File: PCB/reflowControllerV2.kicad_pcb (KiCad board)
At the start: 4 copper layers, 43 x 89 mm, 97 parts, among them J1 CN4, J10 NEXTION_OB, J11 PWR, J12 A-1JB, J2 SSR2, J3 SSR1, J4 FAN1, J5 FAN2, J6 T1, J7 T2, J8 SWD, J9 NEXTION_FRONT, Q1 BSS316NH6327, Q2 BSS316NH6327, Q3 BSS316NH6327, Q4 BSS316NH6327, Q5 BSS316NH6327, SW1 B3F-4055, U1 918-468K2029E50001, U10 ZD24C128A, U2 918-468K2029E50001, U3 AMS1117-3.3, U4 STM32WBxx_QFN48, U5 USBLC6-2SC6, U6 USBLC6-2SC6, U7 CH340G, U8 MAX31855KASA, U9 MAX31855KASA, Y1 NX2016_32MHz, Y2 NX2012_32K768Hz, Y3 12M

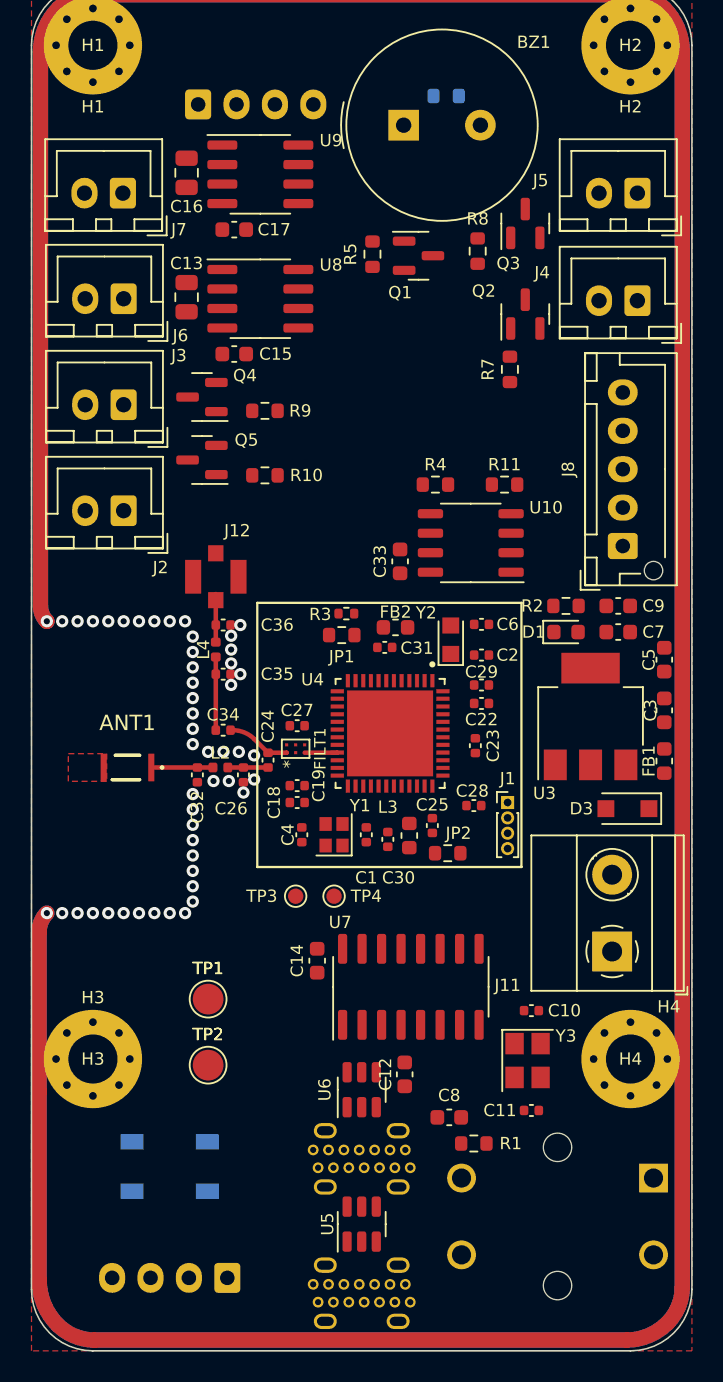
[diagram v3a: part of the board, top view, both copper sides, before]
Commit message: Started layout, critical sections first
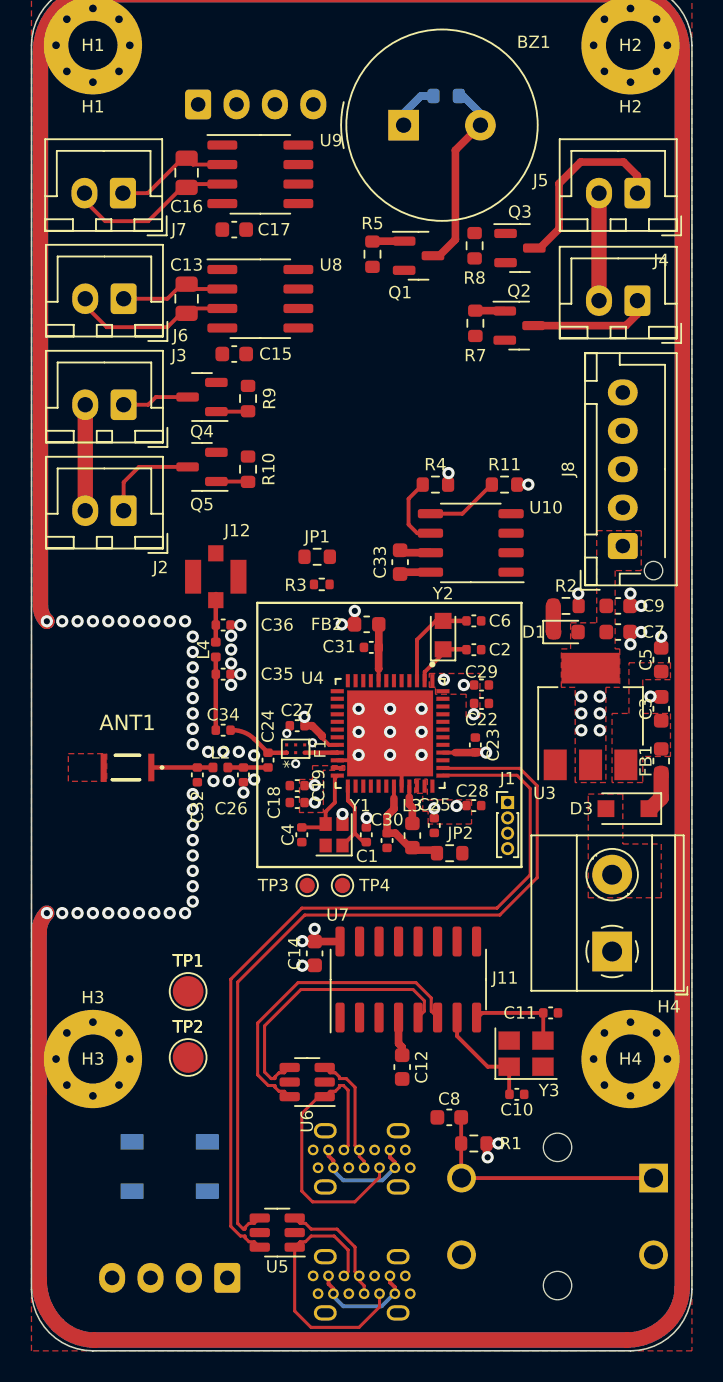
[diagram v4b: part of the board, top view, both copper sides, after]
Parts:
- moved C11 6.47 mm to (33.8, 67.0), turned to 0 degrees
- moved C10 5.53 mm to (31.6, 72.3)
- moved U5 5.53 mm to (16.0, 81.3), turned to 180 degrees
- moved JP1 5.35 mm to (18.6, 37.3)
- moved R7 3.75 mm to (28.9, 22.1)
- moved U6 3.59 mm to (17.9, 71.5), turned to 180 degrees
- moved R3 2.48 mm to (18.9, 39.1)
- moved FB2 1.89 mm to (21.8, 41.7), turned to 0 degrees
- moved Q3 1.64 mm to (31.8, 17.2), turned to 0 degrees
- moved TP1 1.39 mm to (10.2, 65.6)
- moved TP2 1.39 mm to (10.2, 69.9)
- moved R9 1.36 mm to (14.1, 27.0), turned to -90 degrees
- moved R10 1.17 mm to (14.1, 31.6), turned to -90 degrees
- moved TP3 1.03 mm to (17.9, 58.7)
- moved TP4 0.89 mm to (20.2, 58.7)
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- renumbered FILT1 to F1
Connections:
- net Net-(C3-Pad2) renamed /5V_IN
- net Net-(D3-Pad2) renamed /VIN
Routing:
- net /ST_USB_D+: track 0.00 -> 52.6 mm
- net /ST_USB_D-: track 0.00 -> 52.6 mm
- net +3V3: track 0.00 -> 22.0 mm, vias 0 -> 23
- net /UART_USB_D-: track 0.00 -> 20.4 mm
- net /USB2_D-: track 0.00 -> 19.6 mm
- net /UART_USB_D+: track 0.00 -> 18.1 mm
- net /USB1_D-: track 0.00 -> 17.5 mm
- net +5V: track 0.00 -> 16.6 mm
- net /NRST: track 0.00 -> 16.5 mm
- net Net-(BZ1-Pad2): track 0.00 -> 12.7 mm
- net /FAN2: track 0.00 -> 12.3 mm
- net /T2+: track 0.00 -> 11.0 mm
- net /T1+: track 0.00 -> 10.5 mm
- net /USB2_D+: track 0.00 -> 8.06 mm
- net /USB1_D+: track 0.00 -> 7.99 mm
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- added copper zone on F.Cu, net +3V3
- added copper zone on In2.Cu, net +3V3
- added copper zone on F.Cu, net /5V_IN
- added copper zone on F.Cu, net /VIN
- removed copper zone on In2.Cu, net GND

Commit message: Layout done, improovements needed
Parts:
- removed J1: CN4, Connector_PinHeader_1.00mm:PinHeader_1x04_P1.00mm_Vertical
- J10: footprint Connector_JST:JST_XH_S4B-XH-A-1_1x04_P2.50mm_Horizontal -> footprints:JST_254_4P_H
- J2, J3, J4, J5, J6, J7: footprint Connector_JST:JST_XH_B2B-XH-A_1x02_P2.50mm_Vertical -> footprints:JST_254_2P_V
- J8: footprint Connector_JST:JST_XH_B5B-XH-AM_1x05_P2.50mm_Vertical -> footprints:JST_254_5P_V
- J9: footprint Connector_JST:JST_XH_B4B-XH-A_1x04_P2.50mm_Vertical -> footprints:JST_254_4P_V
- moved J12 9.00 mm to (3.00, 38.4), turned to 0 degrees
- moved TP1 7.62 mm to (3.00, 63.1), turned to 90 degrees
- moved TP2 7.39 mm to (7.30, 63.1), turned to 90 degrees
- moved C36 6.93 mm to (6.20, 38.8), turned to 90 degrees
- moved TP4 6.91 mm to (13.5, 57.2)
- moved C35 6.85 mm to (9.40, 38.8), turned to 90 degrees
- moved L4 6.52 mm to (7.80, 38.4), turned to 180 degrees
- moved TP3 5.85 mm to (13.5, 54.9)
- moved Q2 5.06 mm to (32.0, 17.2)
- moved R7 5.06 mm to (29.2, 17.1)
- moved Q3 4.51 mm to (32.0, 21.7)
- moved R8 4.51 mm to (29.1, 21.6)
- moved J2 3.77 mm to (3.25, 31.7), turned to 0 degrees
- moved J3 3.67 mm to (3.25, 25.0), turned to 0 degrees
- moved J6 3.57 mm to (3.25, 18.2), turned to 0 degrees
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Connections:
- J4 pad 1: /FAN1 -> /FAN2
- J5 pad 1: /FAN2 -> /FAN1
- J8 pad 2: /NRST -> /SWDIO
- J8 pad 4: /SWDIO -> /NRST
- U4 pad 26: Net-(J1-Pad1) -> unconnected-(U4-Pad26)
- U4 pad 27: Net-(J1-Pad2) -> unconnected-(U4-Pad27)
- U4 pad 29: /FAN2_IO -> /WS_DATA
- U4 pad 6: /WS_DATA -> /FAN2_IO
- U8 pad 7: /SPI_SO -> /SPI1_MISO
- U9 pad 7: /SPI_SO -> /SPI1_MISO
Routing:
- net +5V: track 16.6 -> 157.5 mm, vias 0 -> 1
- net /USART1_RX: track 0.00 -> 106.5 mm, vias 0 -> 1
- net /USART1_TX: track 0.00 -> 105.4 mm, vias 0 -> 2
- net /NRST: track 16.5 -> 77.3 mm, vias 0 -> 3
- net /SPI1_MISO: track 0.00 -> 42.4 mm
- net /FAN1_IO: track 0.00 -> 41.4 mm, vias 0 -> 2
- net /T2_CS: track 0.00 -> 37.2 mm, vias 0 -> 2
- net /SPI1_SCK: track 0.00 -> 35.1 mm
- net /WS_DATA: track 0.00 -> 33.2 mm, vias 0 -> 1
- net /LPUART1_TX: track 0.00 -> 28.1 mm, vias 0 -> 2
- net /T1_CS: track 0.00 -> 27.9 mm
- net /BUZ: track 0.00 -> 27.1 mm, vias 0 -> 2
- net /LPUART1_RX: track 0.00 -> 26.9 mm, vias 0 -> 2
- net /FAN2_IO: track 0.00 -> 26.3 mm
- net /SWCLK: track 0.00 -> 25.6 mm
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- added copper zone on B.Cu, net GND

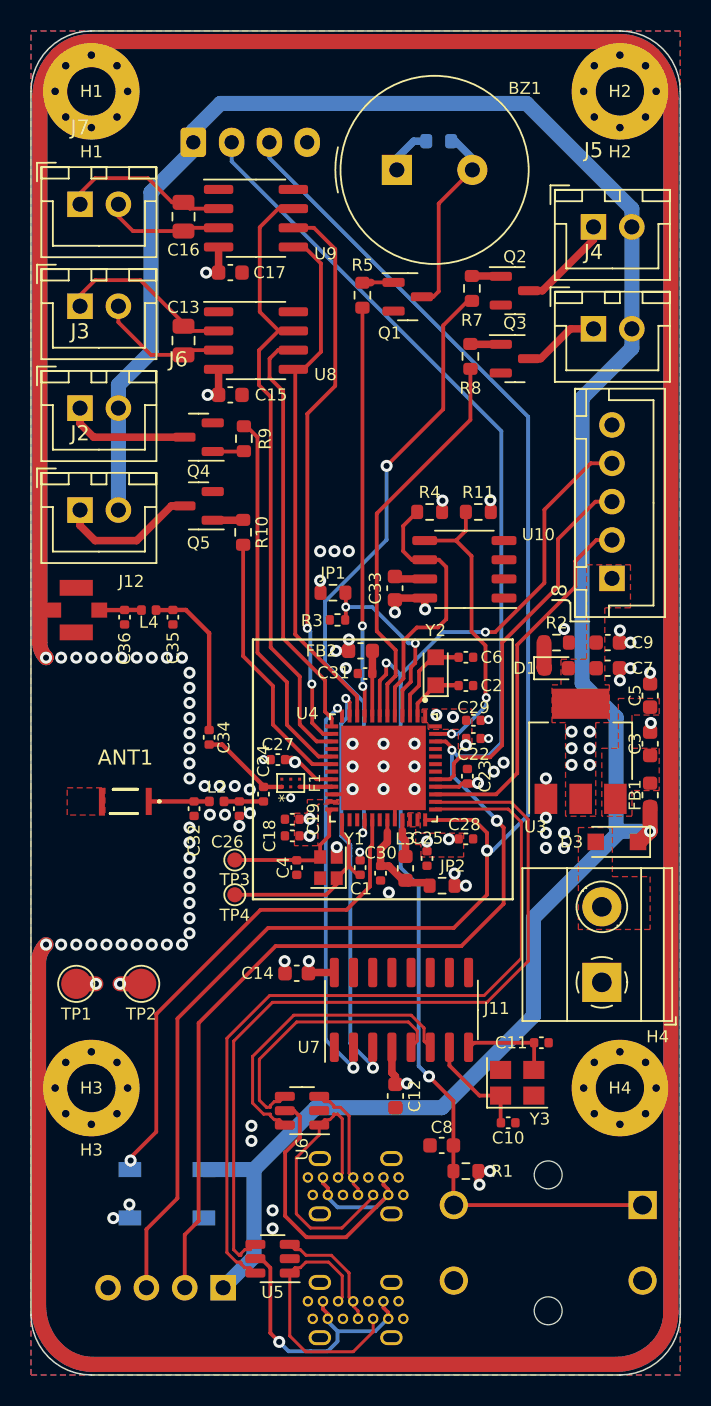
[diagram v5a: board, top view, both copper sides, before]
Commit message: PCB finalized, Gerbers created, Firmware dir renamed
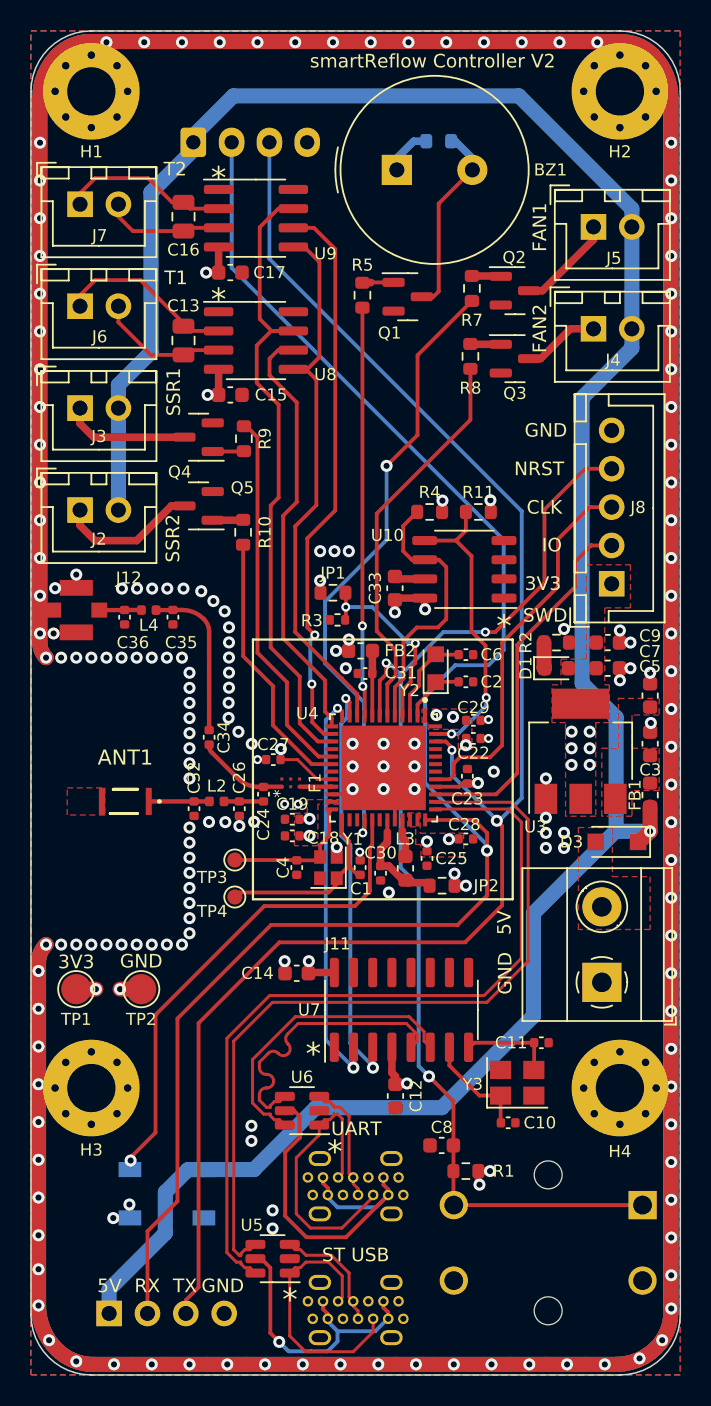
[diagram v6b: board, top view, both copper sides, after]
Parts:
- added REF**: OSHW-Logo_5.7x6mm_SilkScreen, Symbol:OSHW-Logo_5.7x6mm_SilkScreen, B.Cu at (21.5, 42.4)
- added REF**: ESD-Logo_8.9x8mm_SilkScreen, Symbol:ESD-Logo_8.9x8mm_SilkScreen, B.Cu at (17.0, 33.7)
- added REF**: WEEE-Logo_5.6x8mm_SilkScreen, Symbol:WEEE-Logo_5.6x8mm_SilkScreen, B.Cu at (27.4, 33.7)
- moved J9 7.74 mm to (5.17, 84.9), turned to 0 degrees
- moved J8 0.36 mm to (38.5, 36.6)
- moved TP1 0.35 mm to (3.00, 63.5)
- moved TP2 0.35 mm to (7.30, 63.5)
- moved C27 0.30 mm to (16.1, 48.2)
- moved C2 0.25 mm to (28.8, 43.1)
- moved Y2 0.20 mm to (26.8, 42.2)
- moved C6 0.18 mm to (28.8, 41.3)
- moved TP4 0.15 mm to (13.5, 57.4)
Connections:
- J10 pad 2: /USART1_TX -> /USART1_RX
- J10 pad 3: /USART1_RX -> /USART1_TX
- J9 pad 2: /USART1_TX -> /USART1_RX
- J9 pad 3: /USART1_RX -> /USART1_TX
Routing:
- net /USART1_RX: track 106.5 -> 112.3 mm
- net +5V: track 157.5 -> 161.8 mm
- net /USART1_TX: track 105.4 -> 108.6 mm
- net /UART_USB_D+: track 17.9 -> 19.7 mm
- net /SPI1_SCK: track 35.1 -> 36.9 mm
- net /SPI1_MISO: track 42.4 -> 43.4 mm
- net /T1_CS: track 27.9 -> 28.6 mm
- net GND: vias 87 -> 191
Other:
- board text added: "*"
- board text added: "3V3"
- board text added: "5V"
- board text added: "CLK"
- board text added: "Designed by Lukas Walczak"
- board text added: "FAN1"
- board text added: "FAN2"
- board text added: "GND"
- board text added: "IO"
- board text added: "NRST"
- board text added: "RESET"
- board text added: "RX"
- board text added: "SSR1"
- board text added: "SSR2"
- board text added: "ST USB"
- board text added: "SWD"
- board text added: "T1"
- board text added: "T2"
- board text added: "TX"
- board text added: "UART"
- board text added: "smartReflow Controller V2"

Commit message: Recreated Gerbers with removed order number
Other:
- board text added: "JLCJLCJLCJLC"
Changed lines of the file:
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@@
       (outputformat 1)
       (mirror false)
-      (drillshape 1)
+      (drillshape 0)
       (scaleselection 1)
-      (outputdirectory "")
+      (outputdirectory "Gerber/")
     )
   )
@@
     (descr "Open Source Hardware Logo")
     (tags "Logo OSHW")
-    (attr exclude_from_pos_files exclude_from_bom)
+    (attr board_only exclude_from_pos_files exclude_from_bom)
     (fp_text reference "REF**" (at 0 0) (layer "B.SilkS") hide
       (effects (font (size 1 1) (thickness 0.15)) (justify mirror))
@@
     (fp_line (start -0.625 -0.6) (end 0 0.4) (layer "B.Fab") (width 0.1))
     (fp_line (start 0 0.4) (end 0.625 -0.6) (layer "B.Fab") (width 0.1))
-    (pad "1" thru_hole roundrect (at 0 0) (size 1.7 1.95) (drill 0.95) (layers *.Cu *.Mask) (roundrect_rratio 0.147059)
+    (pad "1" thru_hole roundrect (at 0 0) (size 1.7 1.95) (drill 0.95) (layers *.Cu *.Mask) (roundrect_rratio 0.1470588235)
       (net 22 "+5V") (pinfunction "Pin_1") (pintype "passive"))
     (pad "2" thru_hole oval (at 2.54 0) (size 1.7 1.95) (drill 0.95) (layers *.Cu *.Mask)
@@
     (descr "Electrostatic discharge Logo")
     (tags "Logo ESD")
-    (attr exclude_from_pos_files exclude_from_bom)
+    (attr board_only exclude_from_pos_files exclude_from_bom)
     (fp_text reference "REF**" (at 0 0) (layer "B.SilkS") hide
       (effects (font (size 1 1) (thickness 0.15)) (justify mirror))
@@
     (descr "Waste Electrical and Electronic Equipment Directive")
     (tags "Logo WEEE")
-    (attr exclude_from_pos_files exclude_from_bom)
+    (attr board_only exclude_from_pos_files exclude_from_bom)
     (fp_text reference "REF**" (at 0 0) (layer "B.SilkS") hide
       (effects (font (size 1 1) (thickness 0.15)) (justify mirror))
@@
     (effects (font (size 0.9 0.9) (thickness 0.125)) (justify mirror))
   )
+  (gr_text "JLCJLCJLCJLC\n" (at 34.25 80.25) (layer "B.SilkS")
+    (effects (font (size 1 1) (thickness 0.15)) (justify mirror))
+  )
   (gr_text "Designed by Lukas Walczak" (at 21.5 28.3) (layer "B.SilkS")
